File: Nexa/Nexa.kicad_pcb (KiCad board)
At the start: 2 copper layers, 90 x 60 mm, 77 parts, among them J1 Conn_01x04, J10 Conn_01x02_Male, J11 DB9_Female, J12 Conn_01x02_Male, J13 Conn_01x02_Male, J14 Conn_01x01, J15 Conn_01x01, J16 Conn_01x01, J17 Conn_01x01, J18 Conn_01x01, J19 Conn_01x01, J2 Conn_01x02_Male, J20 Conn_01x01, J21 Conn_01x01, J3 Conn_01x04, J4 Conn_02x03_Odd_Even, J5 Conn_01x23, J6 proto_grid_15x21, J7 Conn_02x02_Top_Bottom, J8 Conn_02x02_Top_Bottom, J9 Conn_01x02_Male, Q1 Q_NMOS_DGS, SW1 SW_Push, U1 STM32F103C8, U2 LM1117-5.0, U3 LM1117-3.3, U4 MAX485E, U5 MAX485E, Y1 8 MHz, Y2 32.768 KHz

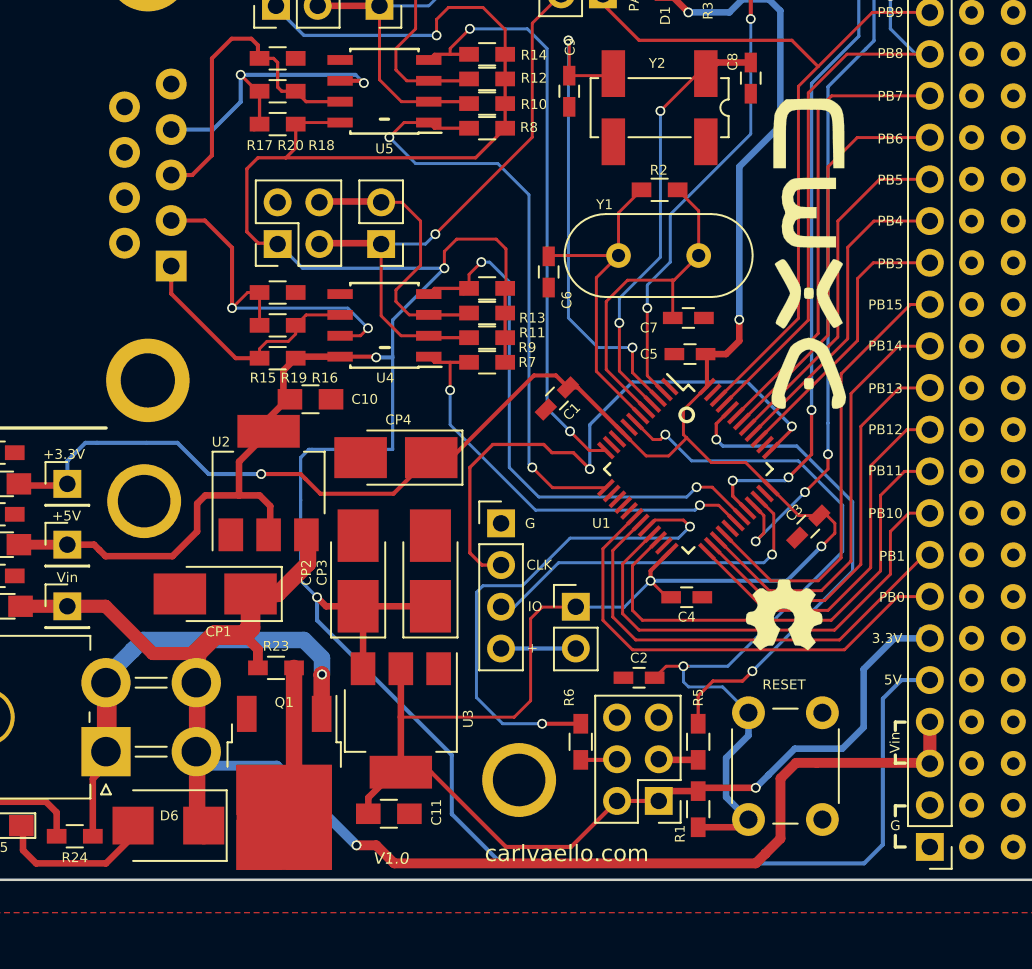
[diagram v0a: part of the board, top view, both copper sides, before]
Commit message: Issue #1 and #2 closed
#1 Polarity protection N_Mosfet is NOT correct configured
Mosfets had incorrect pinout.
#2 CP1 (10nF-16V), max V should be oversize
CP1 is now a 25V cap
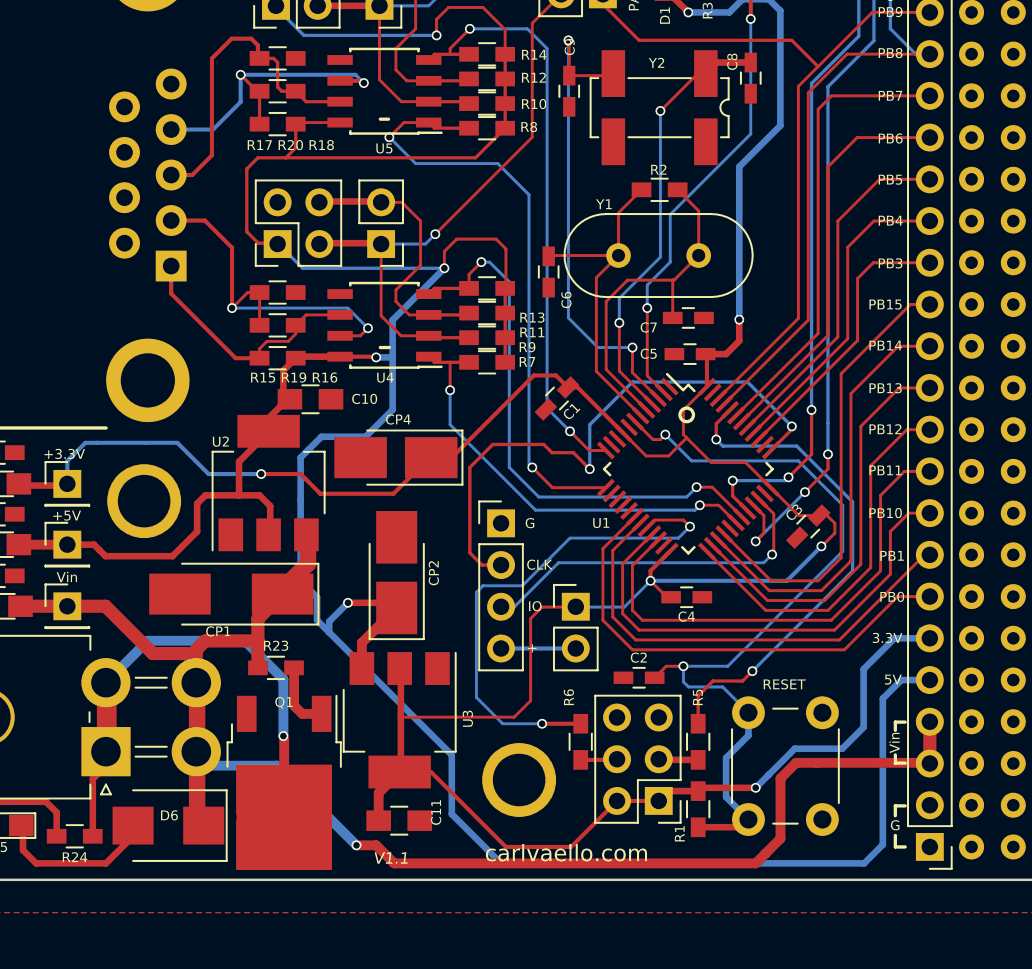
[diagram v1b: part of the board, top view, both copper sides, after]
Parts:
- removed CP3: 10uF, Capacitors_Tantalum_SMD:CP_Tantalum_Case-B_EIA-3528-21_Hand
- removed G***: LOGO, logos:nexa_logo_S-V-22-j
- removed G***: LOGO, logos:oshw_5_4
- CP1: value 10uF -> 10uF - 25V; footprint Capacitors_Tantalum_SMD:CP_Tantalum_Case-B_EIA-3528-21_Hand -> Capacitors_Tantalum_SMD:CP_Tantalum_Case-C_EIA-6032-28_Hand
- CP2: value 22uF -> 22uF - 16V
- CP4: value 22uF -> 22uF - 16 V
- Q1: value Q_NMOS_DGS -> Q_NMOS_GDS
- moved CP2 2.35 mm to (27.4, 41.3)
- moved CP1 0.98 mm to (17.4, 42.6)
- moved C11 0.76 mm to (27.6, 56.4)
- moved U3 0.07 mm to (27.6, 50.3)
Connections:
- Q1 pad 1: POWER_IN-GND -> Net-(Q1-Pad1)
- Q1 pad 2: Net-(Q1-Pad2) -> POWER_IN-GND
- R23 pad 1: Net-(Q1-Pad2) -> Net-(Q1-Pad1)
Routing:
- net Net-(Q1-Pad2): track 12.9 -> 0.00 mm
- net POWER_IN-GND: track 28.4 -> 34.5 mm
- net Net-(Q1-Pad1): track 0.00 -> 4.19 mm
- net +5V: track 204.1 -> 201.7 mm
- net +12V: track 93.2 -> 93.9 mm
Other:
- board text added: "V1.1"
- board text removed: "CP3"
- board text removed: "V1.0"
